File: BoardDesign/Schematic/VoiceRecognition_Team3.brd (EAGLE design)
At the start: 92.7 x 63.5 mm, 52 parts, among them J1 5.5x2.1mm Barrel, Q1 16MHz, X1 USB-A

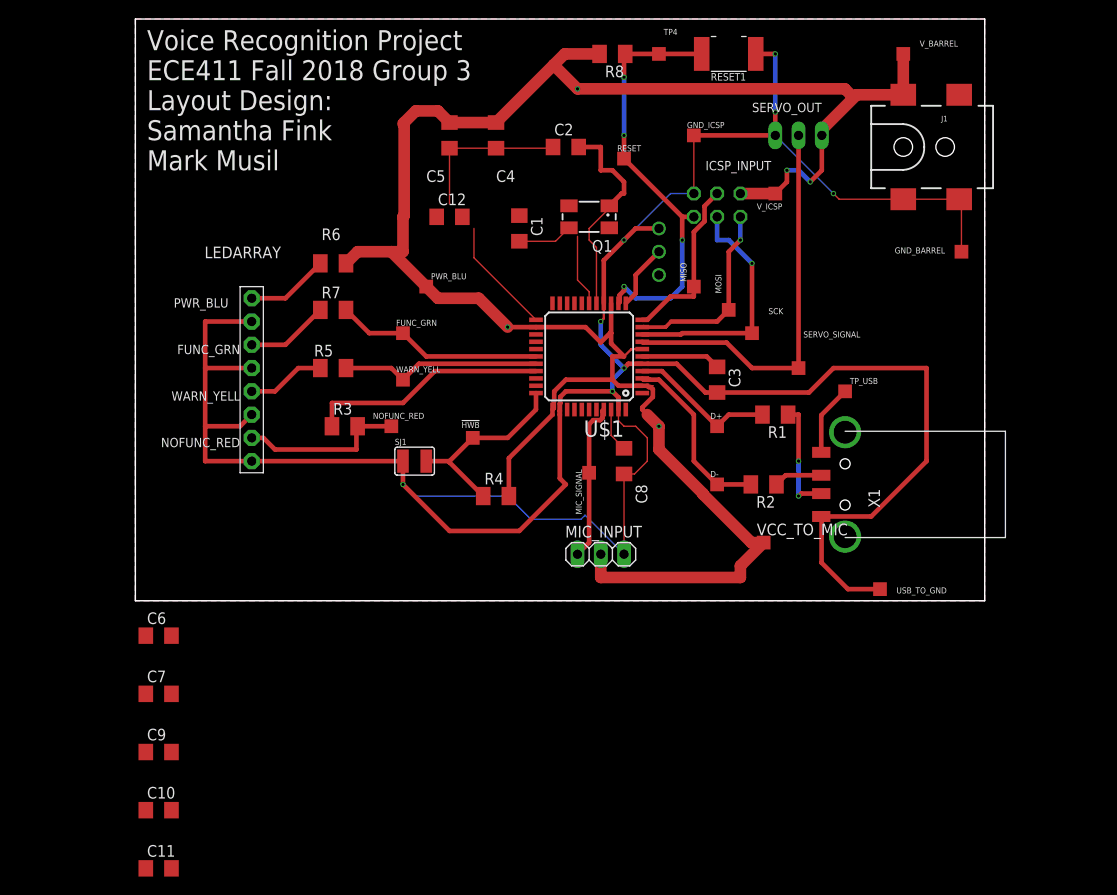
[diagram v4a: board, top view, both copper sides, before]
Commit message: VCC caps + cosmetics
* Moved vcc bias caps onto board.
* Moved component names/values around for legibility.
* Rerouted some wires for cosmetic purposes.
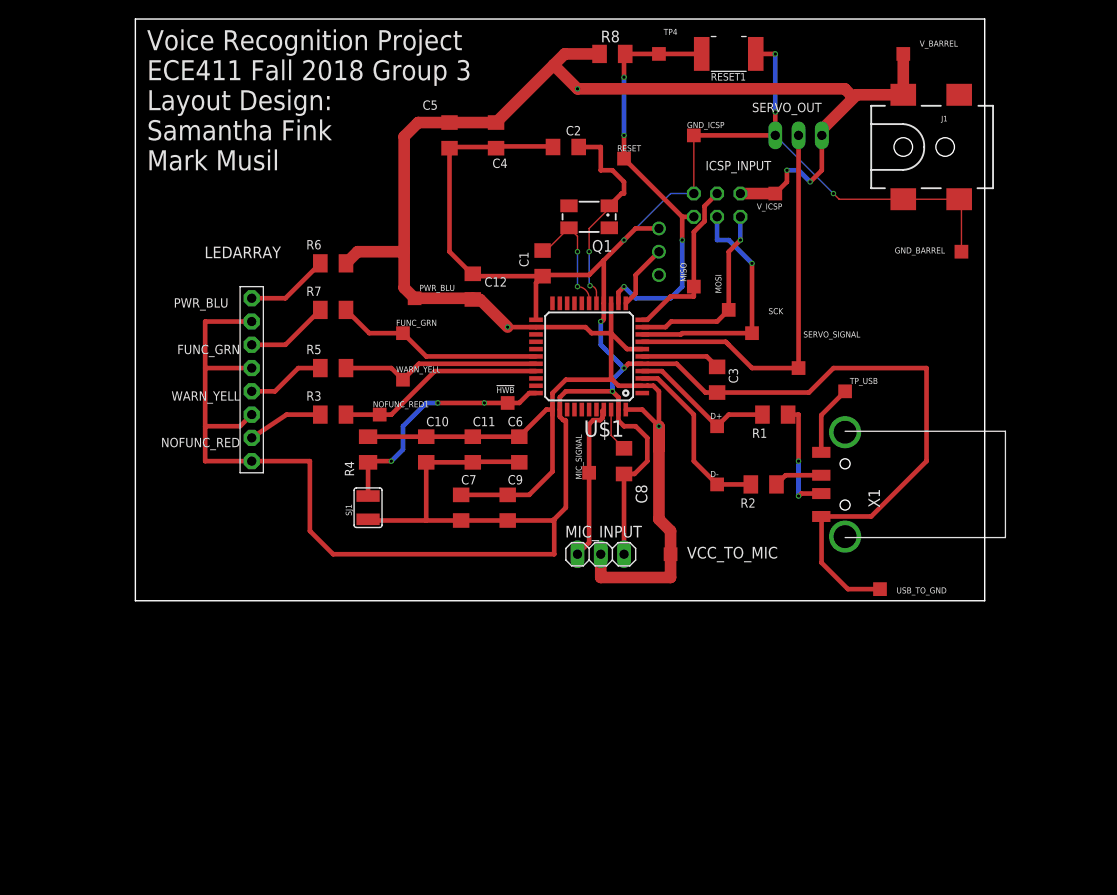
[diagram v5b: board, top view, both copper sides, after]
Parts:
- removed NOFUNC_RED: TPTP15SQ, testpad:TP15SQ
- added NOFUNC_RED1: TPTP15SQ, testpad:TP15SQ
- moved C11 57.1 mm to (49.5, 16.5), turned to 270 degrees
- moved C10 49.0 mm to (44.5, 16.5), turned to 270 degrees
- moved C9 46.5 mm to (53.3, 10.2), turned to 270 degrees
- moved C6 44.3 mm to (54.6, 16.5), turned to 270 degrees
- moved C7 38.8 mm to (48.3, 10.2), turned to 270 degrees
- moved R4 14.9 mm to (38.1, 16.5), turned to 90 degrees
- moved VCC_TO_MIC 10.2 mm to (71.1, 5.08)
- moved C12 8.03 mm to (49.5, 34.3), turned to 90 degrees
- moved SJ1 7.18 mm to (38.1, 10.2), turned to 90 degrees
- moved !HWB 5.39 mm to (53.3, 21.6)
- moved C1 4.58 mm to (57.1, 36.8), turned to 90 degrees
- moved R3 1.80 mm to (34.3, 20.3), turned to 180 degrees
- moved PWR_BLU 1.80 mm to (43.2, 33.0)
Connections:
- net N$6: no longer NOFUNC_RED.TP
- net NOFUNC_RED: now also NOFUNC_RED1.TP
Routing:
- net GND: track 337.3 -> 369.7 mm, vias 8 -> 7
- net VCC: track 226.8 -> 244.5 mm
- net N$6: track 18.2 -> 8.26 mm
- net HWB: track 21.4 -> 26.6 mm, vias 0 -> 3
- net NOFUNC_RED: track 26.3 -> 22.7 mm
- net N$22: track 23.3 -> 23.6 mm, vias 0 -> 2
- net N$2: track 13.9 -> 13.6 mm, vias 0 -> 2
- removed copper zone on layer 1, net GND
- removed copper zone on layer 16, net GND

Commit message: Vias & Ground Plane
*Verified that all vias tied to GND were stiched. Wondering if we need additional ground stitching vias around the board?
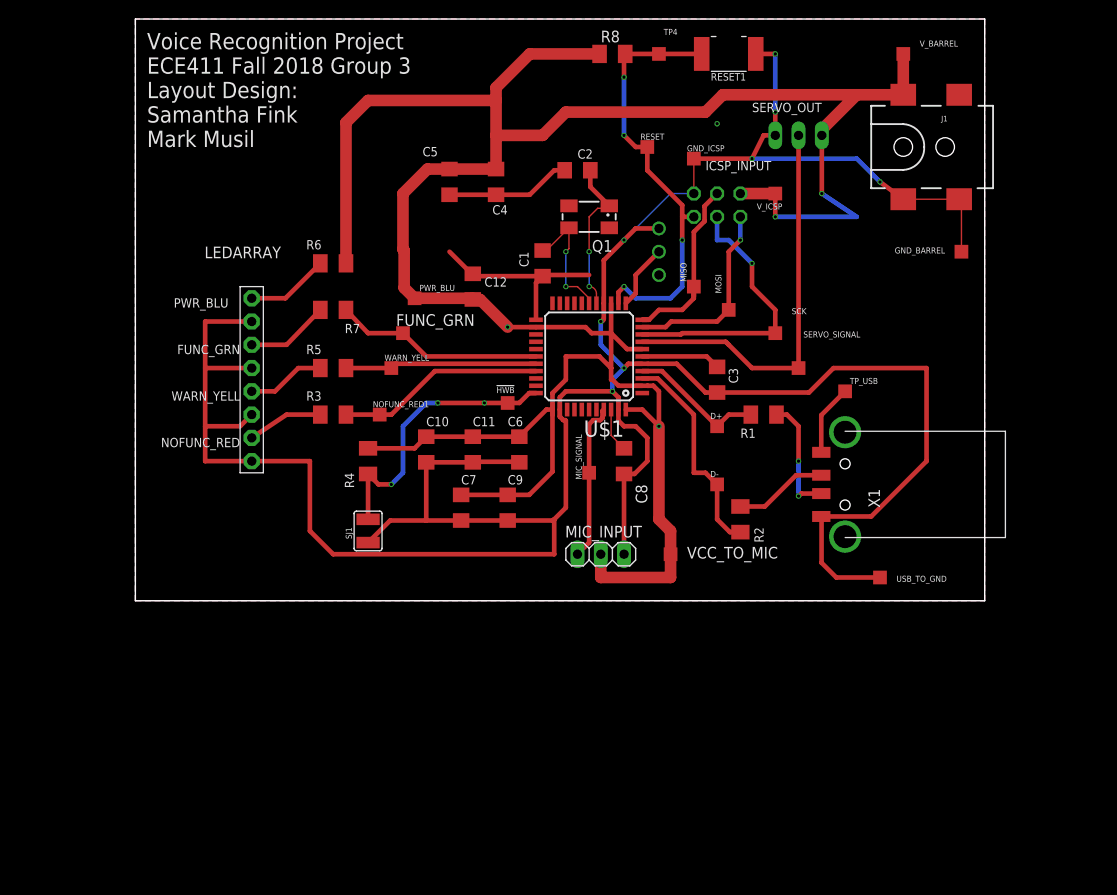
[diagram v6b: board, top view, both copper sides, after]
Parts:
- moved C4 5.08 mm to (52.1, 45.7)
- moved C5 5.08 mm to (47.0, 45.7)
- moved R2 4.58 mm to (78.7, 8.89), turned to 270 degrees
- moved C2 2.84 mm to (61.0, 47.0)
- moved RESET 2.84 mm to (68.6, 49.5)
- moved SJ1 2.54 mm to (38.1, 7.62)
- moved GND_ICSP 2.54 mm to (73.7, 48.3)
- moved SCK 2.54 mm to (82.5, 29.2)
- moved WARN_YELL 1.80 mm to (40.6, 25.4)
- moved R4 1.27 mm to (38.1, 15.2)
- moved USB_TO_GND 1.27 mm to (94.0, 2.54)
- moved R1 1.27 mm to (81.3, 20.3)
- turned R7 to 180 degrees
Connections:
- new net N$8: LEDARRAY.3, R7.2
- net FUNC_GRN: no longer LEDARRAY.3, R7.2
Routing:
- net VCC: track 244.5 -> 288.8 mm, vias 5 -> 4
- net FUNC_GRN: track 34.3 -> 22.9 mm
- net GND: track 369.7 -> 358.7 mm, vias 7 -> 9
- net N$8: track 0.00 -> 9.11 mm
- net N$22: track 23.6 -> 17.4 mm
- net N$9: track 5.30 -> 10.2 mm
- net HWB: track 26.6 -> 30.9 mm
- net N$20: track 19.6 -> 23.6 mm
- net SCK: track 27.2 -> 30.7 mm
- net RST: track 49.9 -> 47.9 mm
- net MISO: track 19.0 -> 20.7 mm
- net N$12: track 16.1 -> 14.9 mm
- net WARN_YELL: track 22.0 -> 20.9 mm
- net N$2: track 13.6 -> 14.6 mm
- net N$3: track 12.6 -> 13.1 mm
- added copper zone on layer 1, net GND
- added copper zone on layer 16, net GND

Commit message: Rearranges
* Moved some components around per Tom's suggestons. Edits from 11/12; forgot to push to git.,
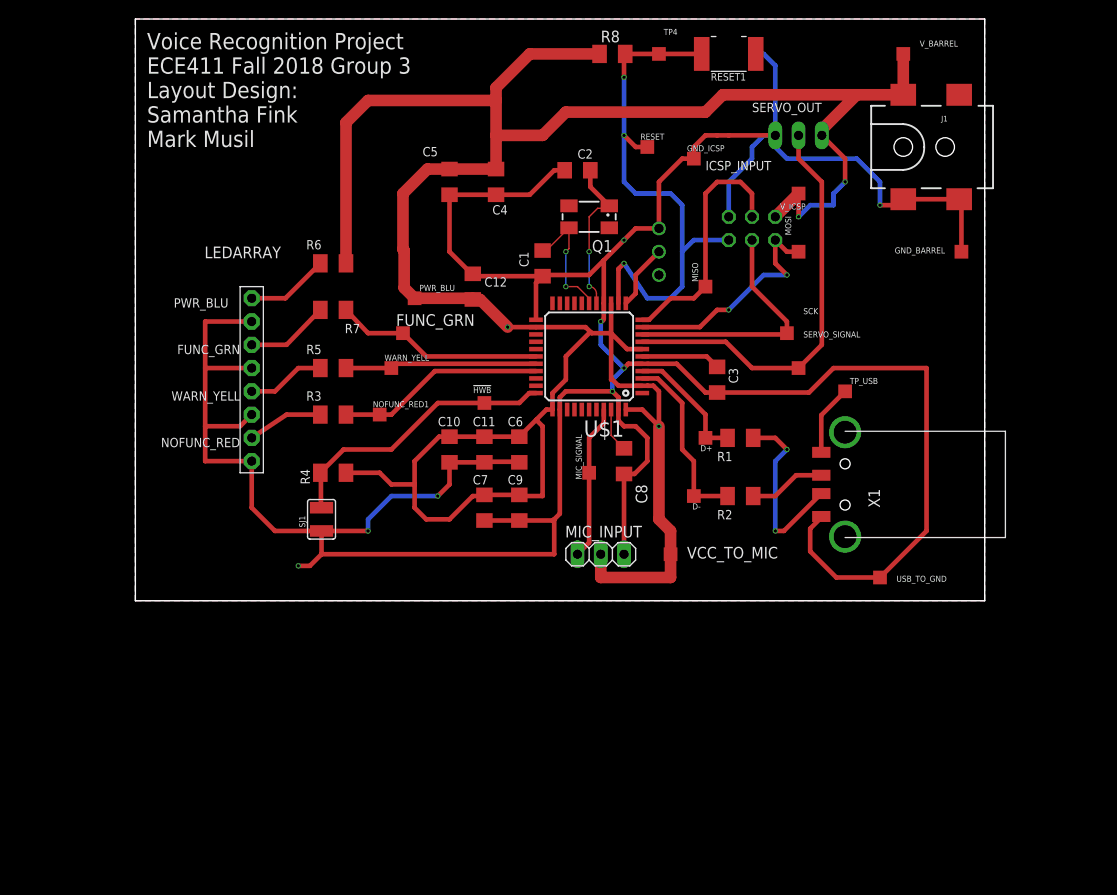
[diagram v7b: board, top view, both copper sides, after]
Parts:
- moved MOSI 9.92 mm to (85.1, 38.1)
- moved SJ1 5.24 mm to (33.0, 8.89)
- moved ICSP_INPUT 4.58 mm to (80.0, 40.6)
- moved R4 4.02 mm to (34.3, 14.0), turned to 0 degrees
- moved R1 3.59 mm to (78.7, 17.8)
- moved D- 2.84 mm to (73.7, 11.4)
- moved !HWB 2.54 mm to (50.8, 21.6)
- moved V_ICSP 2.54 mm to (85.1, 44.5)
- moved C10 2.54 mm to (47.0, 16.5)
- moved C7 2.54 mm to (50.8, 10.2)
- moved R2 2.54 mm to (78.7, 11.4), turned to 180 degrees
- moved D+ 1.80 mm to (74.9, 17.8)
- moved MISO 1.27 mm to (74.9, 34.3)
- moved C11 1.27 mm to (50.8, 16.5)
- moved C9 1.27 mm to (54.6, 10.2)
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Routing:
- net GND: track 358.7 -> 376.2 mm, vias 9 -> 8
- net RST: track 47.9 -> 60.9 mm, vias 4 -> 3
- net N$3: track 13.1 -> 20.3 mm
- net VCC: track 288.8 -> 295.7 mm
- net MISO: track 20.7 -> 27.2 mm
- net MOSI: track 20.9 -> 25.5 mm, vias 1 -> 2
- net N$20: track 23.6 -> 19.8 mm
- net SCK: track 30.7 -> 27.6 mm, vias 1 -> 0
- net SIGNAL: track 43.6 -> 45.8 mm
- net N$9: track 10.2 -> 8.37 mm
- net N$12: track 14.9 -> 13.8 mm
- net HWB: track 30.9 -> 31.0 mm, vias 3 -> 0

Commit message: Additional Board Updates
*Moved C1 so signals N$2 and N$22 (from crystal oscillator) would connect directly to processor instead of through a via. Signal wire is now wider than previous versions of the layout.

* Moved a few GND wires around.

* Added two additional GND stitching vias.
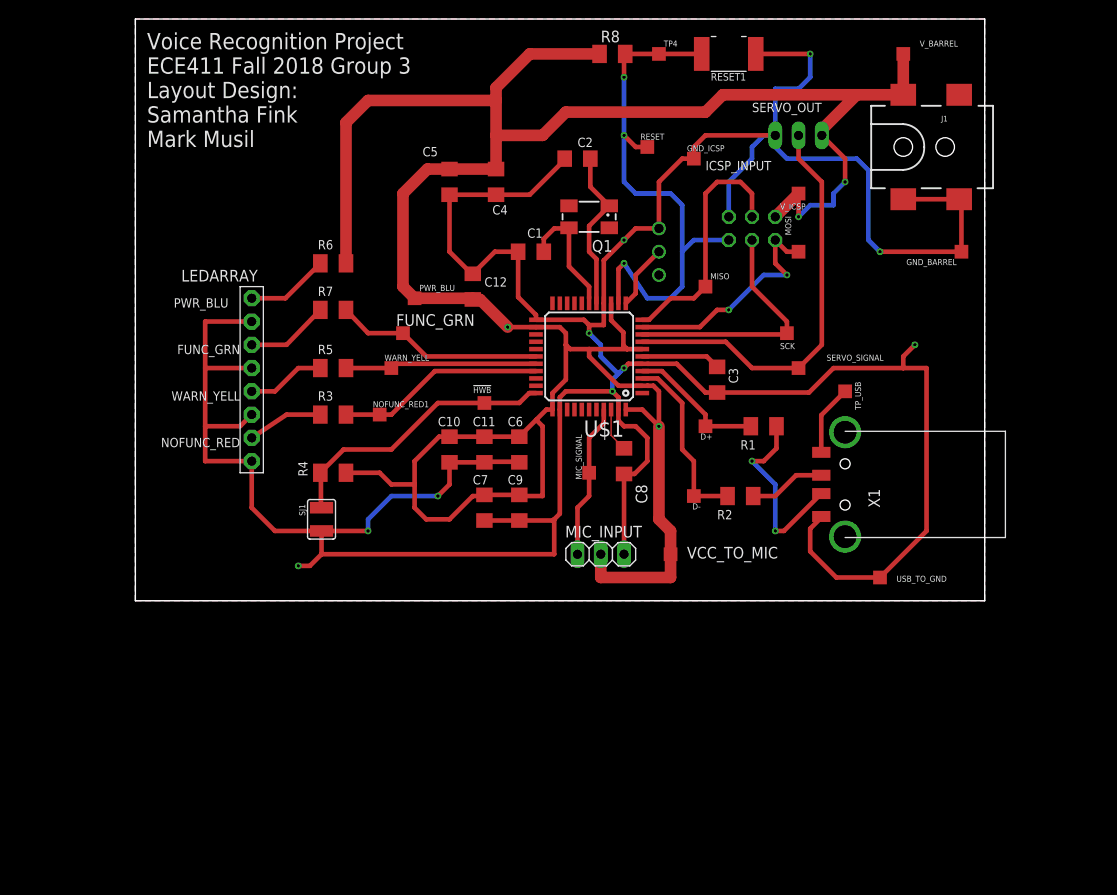
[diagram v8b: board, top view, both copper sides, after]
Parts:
- moved R1 2.84 mm to (81.3, 19.1)
- moved C1 1.80 mm to (55.9, 38.1), turned to 0 degrees
- moved D+ 1.27 mm to (74.9, 19.1)
- moved C2 1.27 mm to (61.0, 48.3)
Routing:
- net GND: track 376.2 -> 400.7 mm, vias 8 -> 10
- net N$12: track 13.8 -> 15.1 mm
- net N$2: track 14.6 -> 13.8 mm, vias 2 -> 0
- net N$3: track 20.3 -> 21.0 mm
- net N$22: track 17.4 -> 17.9 mm, vias 2 -> 0
